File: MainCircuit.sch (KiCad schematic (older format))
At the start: 9 parts, among them Q1 IPA60R280P7S, Q2 IPA60R280P7S, Q3 IPA60R280P7S, Q4 IPA60R280P7S, Q5 IPA60R280P7S, Q6 IPA60R280P7S, Q7 IPA60R280P7S

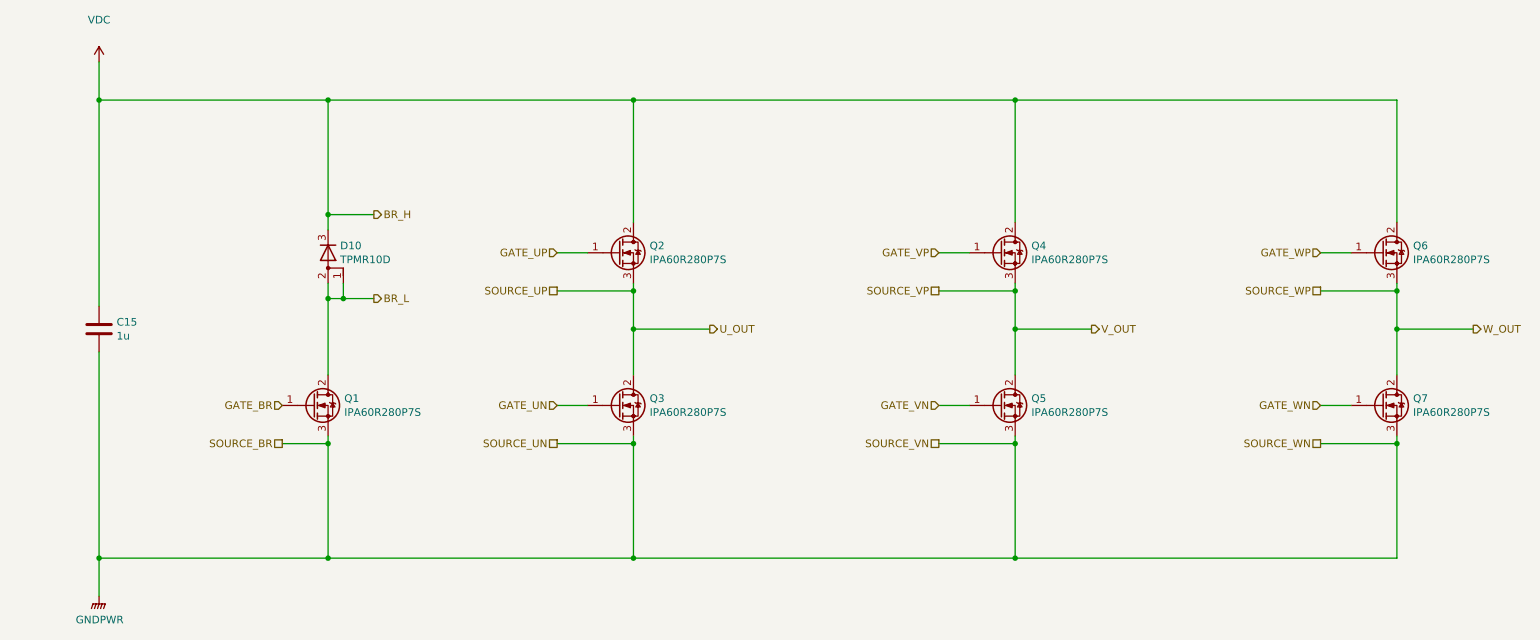
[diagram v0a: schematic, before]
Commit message: テストポイント追加，シルク調整，固定穴マスク追加
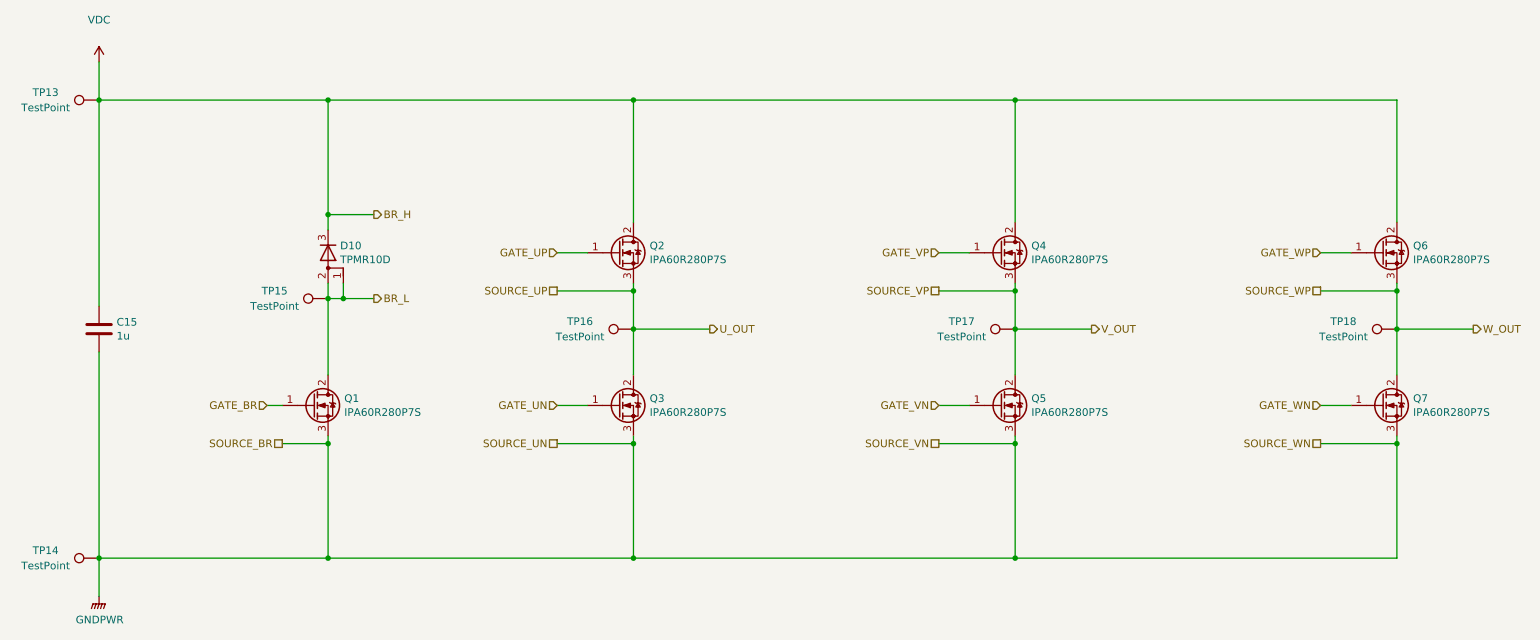
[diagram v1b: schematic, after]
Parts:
- added TP13, TP14, TP15, TP16, TP17, TP18: TestPoint, TestPoint:TestPoint_Loop_D2.50mm_Drill1.0mm_LowProfile, symbol Connector:TestPoint
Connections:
- net BR_L: now also TP15.1
- net GNDPWR: now also TP14.1
- net SOURCE_UP: now also TP16.1
- net SOURCE_VP: now also TP17.1
- net SOURCE_WP: now also TP18.1
- net VDC: now also TP13.1

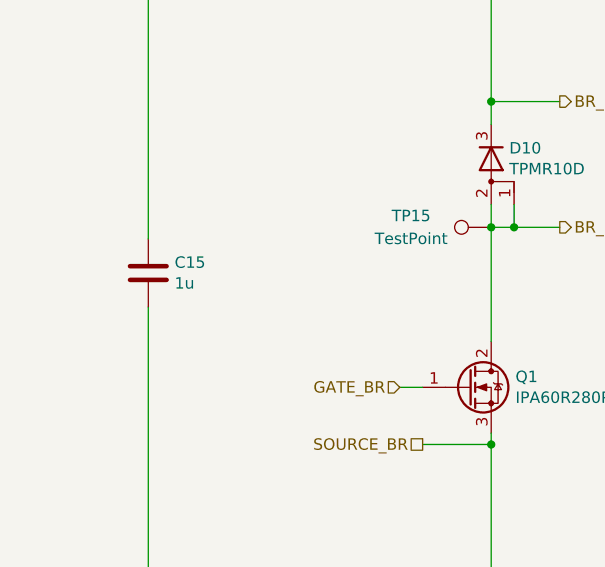
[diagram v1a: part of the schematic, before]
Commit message: DCリンクのフィルムキャパシタの値修正
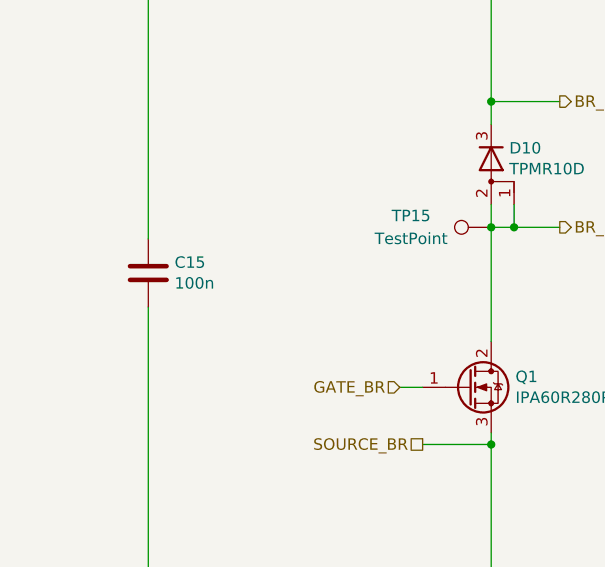
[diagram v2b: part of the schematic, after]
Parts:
- C15: value 1u -> 100n
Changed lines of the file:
@@
 P 1500 3000
 F 0 "C15" H 1615 3046 50  0000 L CNN
-F 1 "1u" H 1615 2955 50  0000 L CNN
+F 1 "100n" H 1615 2955 50  0000 L CNN
 F 2 "Capacitor_THT:C_Rect_L13.0mm_W6.0mm_P10.00mm_FKS3_FKP3_MKS4" H 1538 2850 50  0001 C CNN
 F 3 "~" H 1500 3000 50  0001 C CNN
